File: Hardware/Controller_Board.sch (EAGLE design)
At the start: 14 parts, among them Q7 3.6864MHz, U1 ATMEGA328P-PU, U2 REF3020AIDBZT

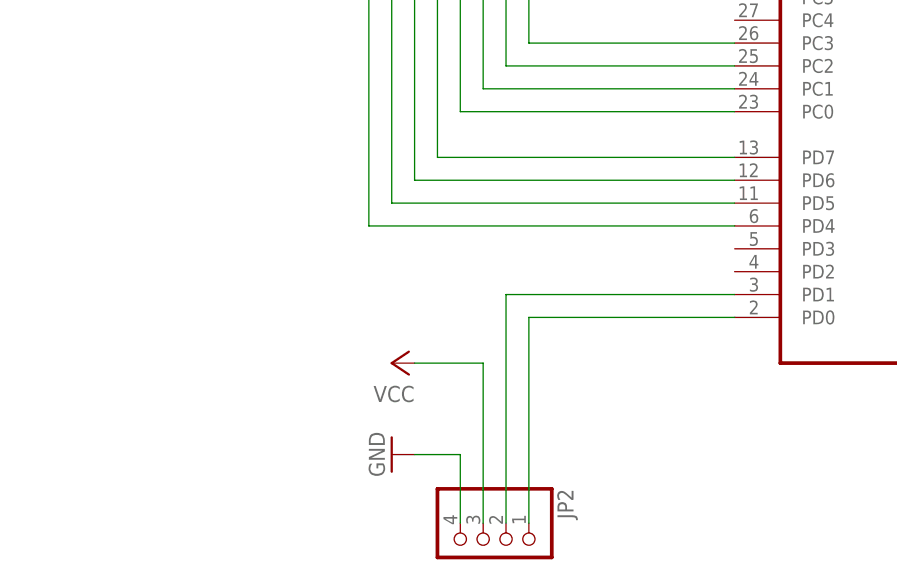
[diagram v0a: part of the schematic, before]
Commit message: Added a status led on the controller board.
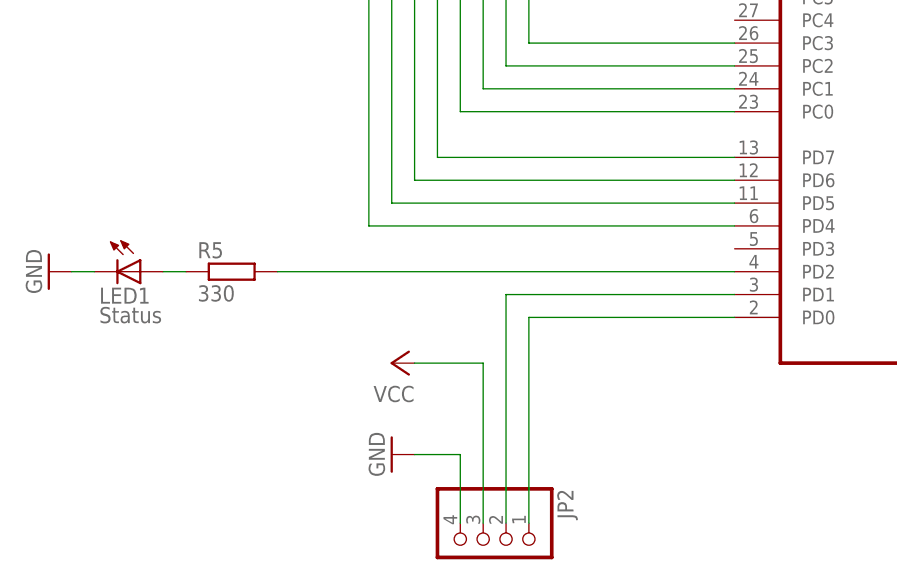
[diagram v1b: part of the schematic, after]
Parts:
- added LED1: Status, led:LED5MM
- added R5: 330, resistor:R-EU_0207/10
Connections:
- new net N$11: R5.2, U1.PD2
- new net N$12: LED1.A, R5.1
- net GND: now also LED1.C
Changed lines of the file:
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@@
 <part name="GND2" library="supply1" deviceset="GND" device=""/>
 <part name="P+7" library="supply1" deviceset="VCC" device=""/>
+<part name="LED1" library="led" deviceset="LED" device="5MM" value="Status"/>
+<part name="GND3" library="supply1" deviceset="GND" device=""/>
+<part name="R5" library="resistor" deviceset="R-EU_" device="0207/10" value="330"/>
 </parts>
 <sheets>
@@
 <instance part="GND2" gate="1" x="-2.54" y="124.46" rot="R270"/>
 <instance part="P+7" gate="VCC" x="-2.54" y="134.62" rot="R90"/>
+<instance part="LED1" gate="G$1" x="-30.48" y="144.78" rot="R270"/>
+<instance part="GND3" gate="1" x="-40.64" y="144.78" rot="R270"/>
+<instance part="R5" gate="G$1" x="-20.32" y="144.78"/>
 </instances>
 <busses>
@@
 <pinref part="JP2" gate="A" pin="4"/>
 <wire x1="5.08" y1="124.46" x2="5.08" y2="116.84" width="0.1524" layer="91"/>
+</segment>
+<segment>
+<pinref part="LED1" gate="G$1" pin="C"/>
+<pinref part="GND3" gate="1" pin="GND"/>
+<wire x1="-35.56" y1="144.78" x2="-38.1" y2="144.78" width="0.1524" layer="91"/>
 </segment>
 </net>
@@
 </segment>
 </net>
+<net name="N$11" class="0">
+<segment>
+<pinref part="U1" gate="A" pin="PD2"/>
+<pinref part="R5" gate="G$1" pin="2"/>
+<wire x1="35.56" y1="144.78" x2="-15.24" y2="144.78" width="0.1524" layer="91"/>
+</segment>
+</net>
+<net name="N$12" class="0">
+<segment>
+<pinref part="R5" gate="G$1" pin="1"/>
+<pinref part="LED1" gate="G$1" pin="A"/>
+<wire x1="-25.4" y1="144.78" x2="-27.94" y2="144.78" width="0.1524" layer="91"/>
+</segment>
+</net>

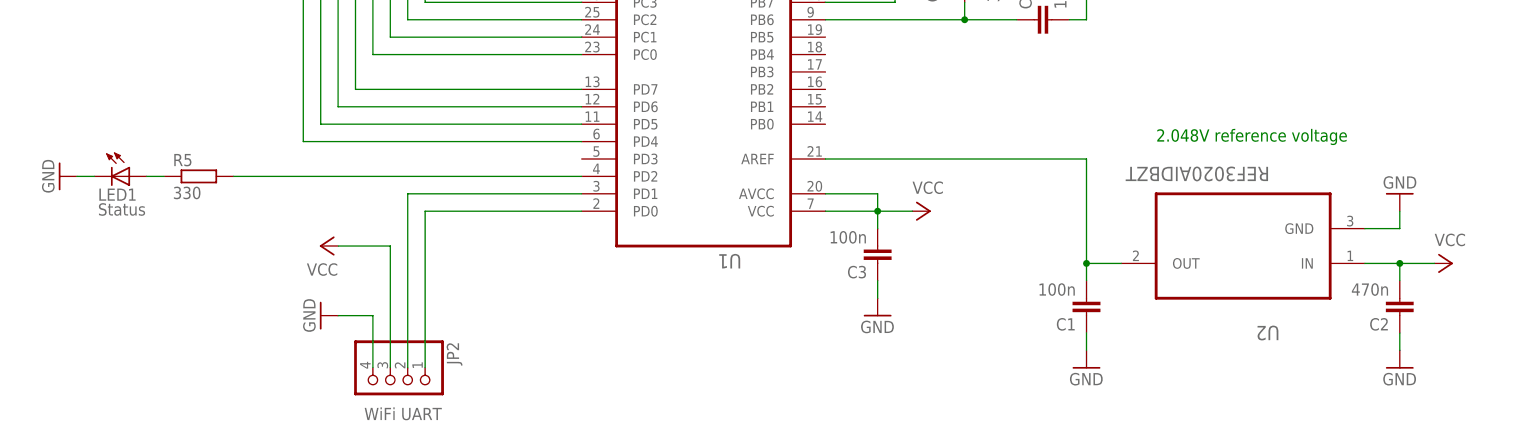
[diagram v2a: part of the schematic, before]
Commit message: Added one more decoupling capacitor close to the control board microcontroller, changed 15pF capacitors package to the good one, added a second led just in case.
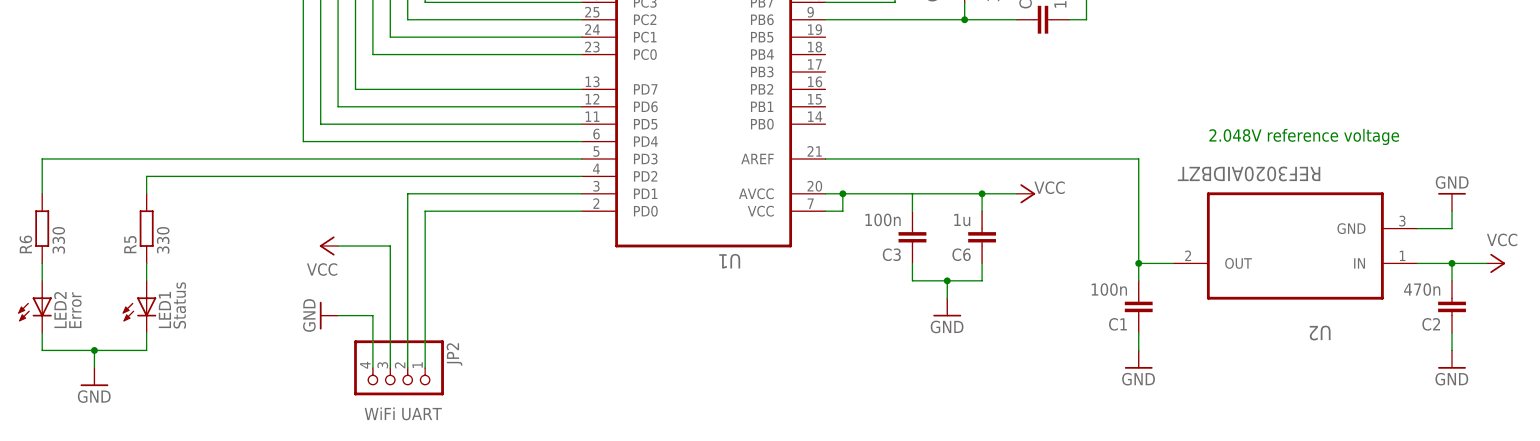
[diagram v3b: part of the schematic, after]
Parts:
- added C6: 1u, rcl:C-EU050-035X075
- added LED2: Error, led:LED5MM
- added R6: 330, resistor:R-EU_0207/10
- C4, C5: device rcl:C-EU025-030X050 -> rcl:C-EU025-050X050
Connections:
- new net N$11: LED2.A, R6.1
- new net N$13: R6.2, U1.PD3
- net GND: now also C6.1, LED2.C
- net VCC: now also C6.2
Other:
- moved on the sheet: C1, C2, C3, LED1, R5, U2
